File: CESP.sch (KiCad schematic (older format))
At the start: 5 parts

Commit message: first draft
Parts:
- removed U?: LTC1594CS, TSSOP14, symbol LTC1594CS
- removed U?: TL074, TSSOP14, symbol TL074
- removed U? (x3): TL074, symbol TL074
- added C? (x2): C, symbol C
- added Conn?: ATX_POWER, symbol ATX_POWER
- added D?: DIODE, symbol DIODE
- added D?: LED, symbol LED
- added IC?: ATTINY87-AX, TSSOP20, symbol ATTINY87-AX
- added P?: CONN_10X2, symbol CONN_10X2
- added Q?: NPN, symbol NPN
- added R? (x3): R, symbol R
- added U?: LT3757EMSE, symbol LT3757EMSE
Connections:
- net labels added: +3,3V
- wire segments 0 -> 14
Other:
- note removed: "NOTE: THIS IS JUST A TEST BOARD\nREMOVE ALL COMPONENTS AND CREATE YOUR OWN\nINCLUDE SCHEMATIC HOOKUPS/NETLIST"
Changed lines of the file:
@@
-EESchema Schematic File Version 2  date 1/24/2014 12:04:40 AM
+EESchema Schematic File Version 2  date man 27 jan 2014 22:27:38 CET
 LIBS:power
 LIBS:device
@@
 LIBS:contrib
 LIBS:valves
+LIBS:ATTINY87-AX
+LIBS:ATX_POWER
 LIBS:CESP-cache
-EELAYER 27 0
+LIBS:LT3757EMSE
+LIBS:CESP-cache
+EELAYER 25  0
 EELAYER END
-$Descr A4 11693 8268
+$Descr A4 11700 8267
 encoding utf-8
 Sheet 1 1
 Title ""
-Date "24 jan 2014"
+Date "27 jan 2014"
 Rev ""
 Comp ""
@@
 Comment4 ""
 $EndDescr
+Connection ~ 2950 5350
+Wire Wire Line
+	2950 5350 2950 5150
+Wire Wire Line
+	2950 5150 1500 5150
+Wire Wire Line
+	3950 4600 3000 4600
+Wire Wire Line
+	2950 3350 2950 3950
+Wire Wire Line
+	2950 3950 1500 3950
+Wire Wire Line
+	1650 1700 1300 1700
+Wire Wire Line
+	1300 1700 1300 1550
+Wire Wire Line
+	1500 4750 1500 4450
+Wire Wire Line
+	2750 5700 2750 5350
+Wire Wire Line
+	2750 5350 3950 5350
+Wire Wire Line
+	3950 5350 3950 5000
+Wire Wire Line
+	2600 4600 2600 4300
+Wire Wire Line
+	2600 4300 5550 4300
+Wire Wire Line
+	5550 4300 5550 4450
 $Comp
-L LTC1594CS U?
-U 1 1 52E1F38F
-P 3750 3300
-F 0 "U?" H 3750 3950 60  0000 C CNN
-F 1 "LTC1594CS" H 3750 2650 60  0000 C CNN
-F 2 "TSSOP14" H 3750 3300 60  0000 C CNN
-F 3 "" H 3750 3300 60  0000 C CNN
-	1    3750 3300
+L CONN_10X2 P?
+U 1 1 52E6C8FE
+P 2050 2050
+F 0 "P?" H 2050 2600 60  0000 C CNN
+F 1 "CONN_10X2" V 2050 1950 50  0000 C CNN
+	1    2050 2050
 	1    0    0    -1
 $EndComp
 $Comp
-L TL074 U?
-U 1 1 52E1F3CD
-P 7150 2150
-F 0 "U?" H 7200 2350 60  0000 C CNN
-F 1 "TL074" H 7300 1950 50  0000 C CNN
-F 2 "TSSOP14" H 7150 2150 60  0000 C CNN
-F 3 "" H 7150 2150 60  0000 C CNN
-	1    7150 2150
+L +3,3V #PWR01
+U 1 1 52E6C85A
+P 1300 1550
+F 0 "#PWR01" H 1300 1510 30  0001 C CNN
+F 1 "+3,3V" H 1300 1660 30  0000 C CNN
+	1    1300 1550
 	1    0    0    -1
 $EndComp
 $Comp
-L TL074 U?
-U 2 1 52E1F3DA
-P 7200 3500
-F 0 "U?" H 7250 3700 60  0000 C CNN
-F 1 "TL074" H 7350 3300 50  0000 C CNN
-F 2 "" H 7200 3500 60  0000 C CNN
-F 3 "" H 7200 3500 60  0000 C CNN
-	2    7200 3500
+L C C?
+U 1 1 52E6C755
+P 1500 4950
+F 0 "C?" H 1550 5050 50  0000 L CNN
+F 1 "C" H 1550 4850 50  0000 L CNN
+	1    1500 4950
 	1    0    0    -1
 $EndComp
 $Comp
-L TL074 U?
-U 1 1 52E1F3E5
-P 8600 3500
-F 0 "U?" H 8650 3700 60  0000 C CNN
-F 1 "TL074" H 8750 3300 50  0000 C CNN
-F 2 "" H 8600 3500 60  0000 C CNN
-F 3 "" H 8600 3500 60  0000 C CNN
-	1    8600 3500
+L C C?
+U 1 1 52E6C752
+P 1100 4950
+F 0 "C?" H 1150 5050 50  0000 L CNN
+F 1 "C" H 1150 4850 50  0000 L CNN
+	1    1100 4950
 	1    0    0    -1
 $EndComp
 $Comp
-L TL074 U?
-U 1 1 52E1F3EB
-P 8550 2100
-F 0 "U?" H 8600 2300 60  0000 C CNN
-F 1 "TL074" H 8700 1900 50  0000 C CNN
-F 2 "" H 8550 2100 60  0000 C CNN
-F 3 "" H 8550 2100 60  0000 C CNN
-	1    8550 2100
+L R R?
+U 1 1 52E6C742
+P 2000 4250
+F 0 "R?" V 2080 4250 50  0000 C CNN
+F 1 "R" V 2000 4250 50  0000 C CNN
+	1    2000 4250
 	1    0    0    -1
 $EndComp
-Text Notes 4450 4650 0    80   ~ 0
-NOTE: THIS IS JUST A TEST BOARD\nREMOVE ALL COMPONENTS AND CREATE YOUR OWN\nINCLUDE SCHEMATIC HOOKUPS/NETLIST
+$Comp
+L R R?
+U 1 1 52E6C73E
+P 1500 4200
+F 0 "R?" V 1580 4200 50  0000 C CNN
+F 1 "R" V 1500 4200 50  0000 C CNN
+	1    1500 4200
+	1    0    0    -1
+$EndComp
+$Comp
+L R R?
+U 1 1 52E6C738
+P 1100 4250
+F 0 "R?" V 1180 4250 50  0000 C CNN
+F 1 "R" V 1100 4250 50  0000 C CNN
+	1    1100 4250
+	1    0    0    -1
+$EndComp
+$Comp
+L NPN Q?
+U 1 1 52E6C72B
+P 3850 4800
+F 0 "Q?" H 3850 4650 50  0000 R CNN
+F 1 "NPN" H 3850 4950 50  0000 R CNN
+	1    3850 4800
+	1    0    0    -1
+$EndComp
+$Comp
+L LED D?
+U 1 1 52E6C716
+P 2800 4600
+F 0 "D?" H 2800 4700 50  0000 C CNN
+F 1 "LED" H 2800 4500 50  0000 C CNN
+	1    2800 4600
+	1    0    0    -1
+$EndComp
+$Comp
+L DIODE D?
+U 1 1 52E6C704
+P 1700 3300
+F 0 "D?" H 1700 3400 40  0000 C CNN
+F 1 "DIODE" H 1700 3200 40  0000 C CNN
+	1    1700 3300
+	1    0    0    -1
+$EndComp
+$Comp
+L LT3757EMSE U?
+U 1 1 52E6C696
+P 5550 5100
+F 0 "U?" H 5700 5600 60  0000 C CNN
+F 1 "LT3757EMSE" H 5950 4600 60  0000 C CNN
+	1    5550 5100
+	1    0    0    -1
+$EndComp
+$Comp
+L ATX_POWER Conn?
+U 1 1 52E6C683
+P 2300 6100
+F 0 "Conn?" H 3050 6100 60  0000 C CNN
+F 1 "ATX_POWER" H 2300 6100 60  0000 C CNN
+	1    2300 6100
+	1    0    0    -1
+$EndComp
+$Comp
+L ATTINY87-AX IC?
+U 1 1 52E6C674
+P 4100 2550
+F 0 "IC?" H 3250 3500 60  0000 C CNN
+F 1 "ATTINY87-AX" H 4750 1600 60  0000 C CNN
+F 2 "TSSOP20" H 3350 1600 60  0001 C CNN
+	1    4100 2550
+	1    0    0    -1
+$EndComp
 $EndSCHEMATC

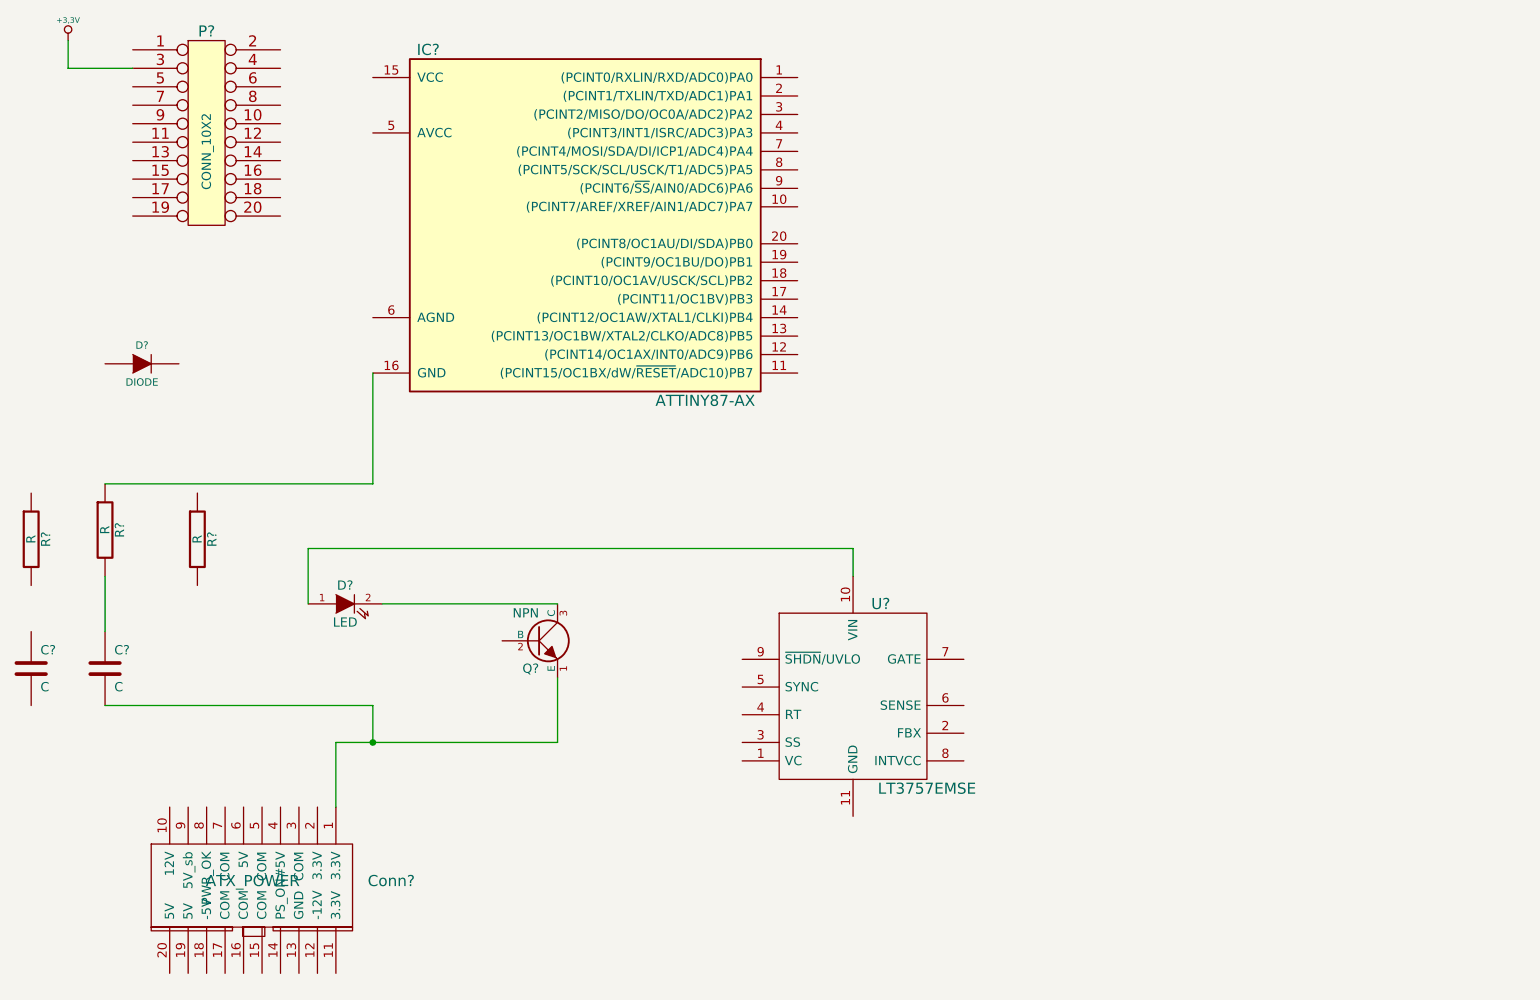
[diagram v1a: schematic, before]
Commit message: new solder board
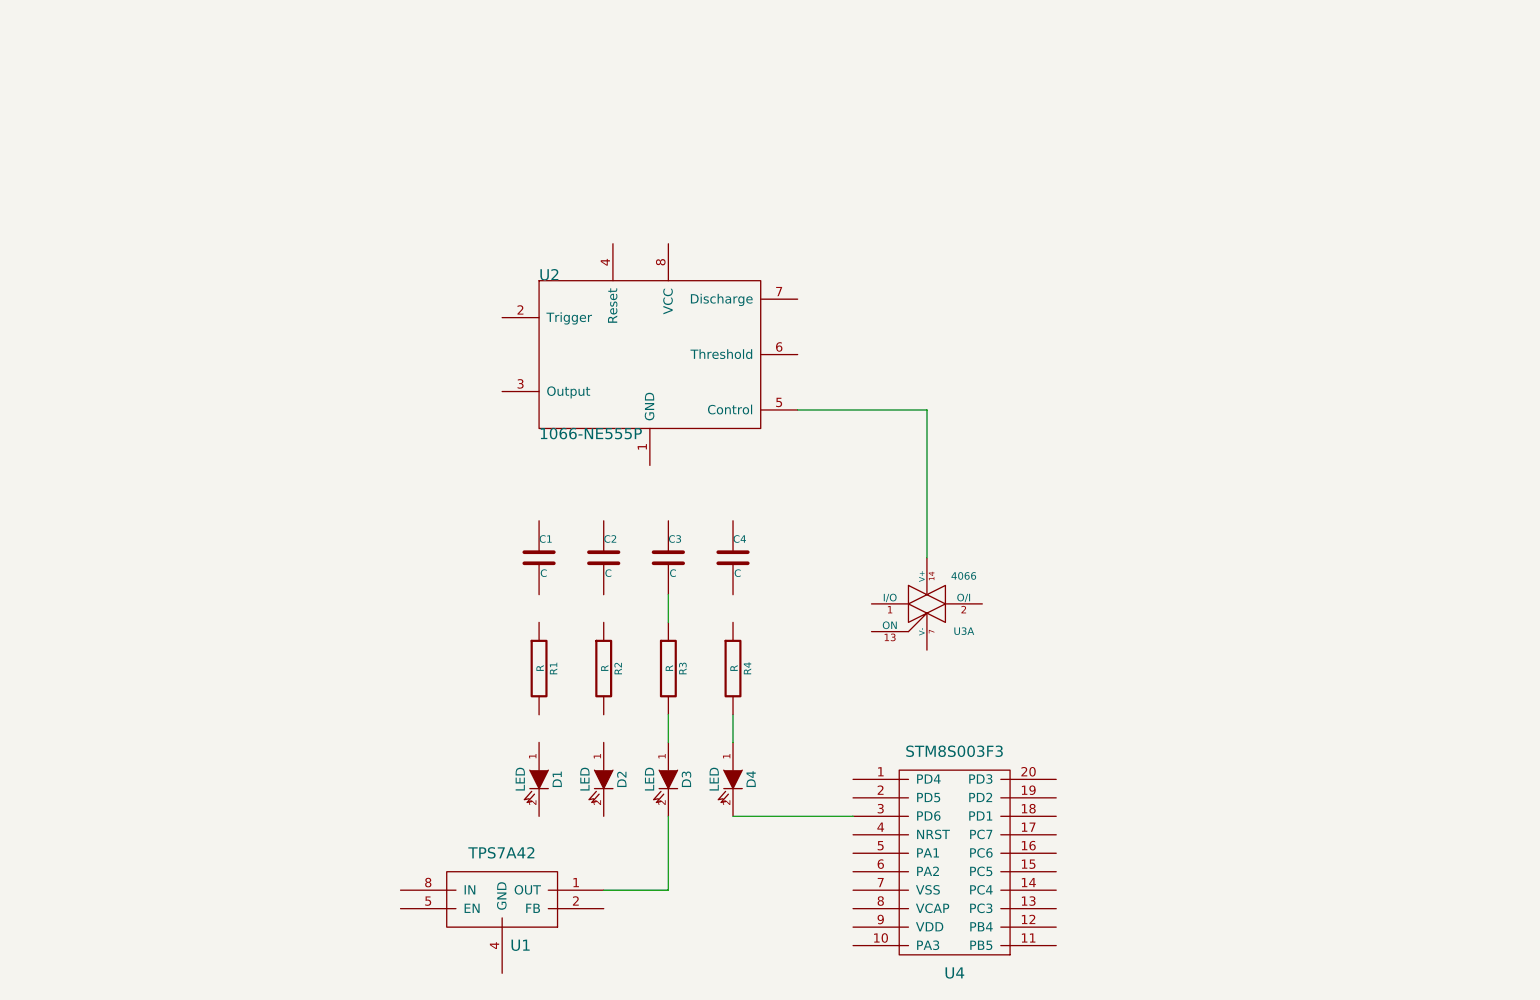
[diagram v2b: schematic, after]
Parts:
- removed C? (x2): C, symbol C
- removed Conn?: ATX_POWER, symbol ATX_POWER
- removed D?: DIODE, symbol DIODE
- removed D?: LED, symbol LED
- removed IC?: ATTINY87-AX, TSSOP20, symbol ATTINY87-AX
- removed P?: CONN_10X2, symbol CONN_10X2
- removed Q?: NPN, symbol NPN
- removed R? (x3): R, symbol R
- removed U?: LT3757EMSE, symbol LT3757EMSE
- added C1, C2, C3, C4: C, ~, symbol C
- added D1, D2, D3, D4: LED, ~, symbol LED
- added R1, R2, R3, R4: R, ~, symbol R
- added U1: TPS7A42, symbol TPS7A42
- added U2: 1066-NE555P, andrew/b6d66, symbol 1066-NE555P
- added U3: 4066, symbol 4066
- added U4: STM8S003F3, ~, symbol STM8S003F3
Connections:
- new net: U2.5 (Control), U3.14 (V+)
- new net: D3.2 (K), U1.1 (OUT)
- new net: D4.2 (K), U4.3 (PD6)
- new net: C3.2, R3.1
- new net: D3.1 (A), R3.2
- new net: D4.1 (A), R4.2
